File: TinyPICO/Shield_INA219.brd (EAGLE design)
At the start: 31.9 x 17.8 mm, 13 parts, among them J1 3.5mm, U1 INA219BIDCNT

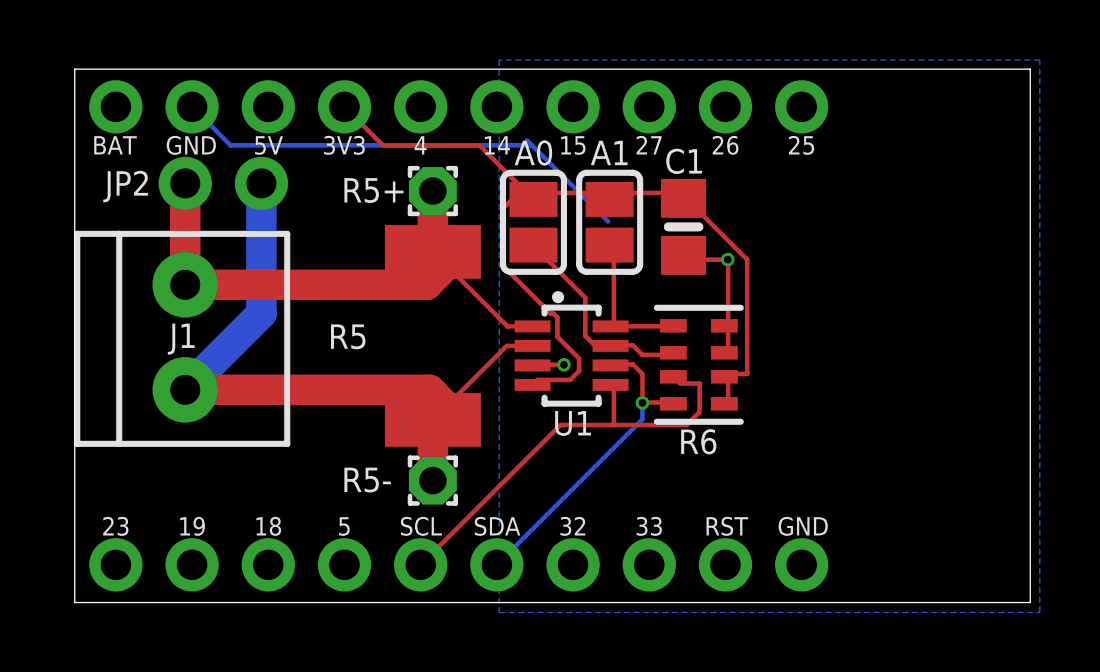
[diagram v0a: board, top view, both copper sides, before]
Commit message: TinyPICO Shield Ammeter INA219 v2.1
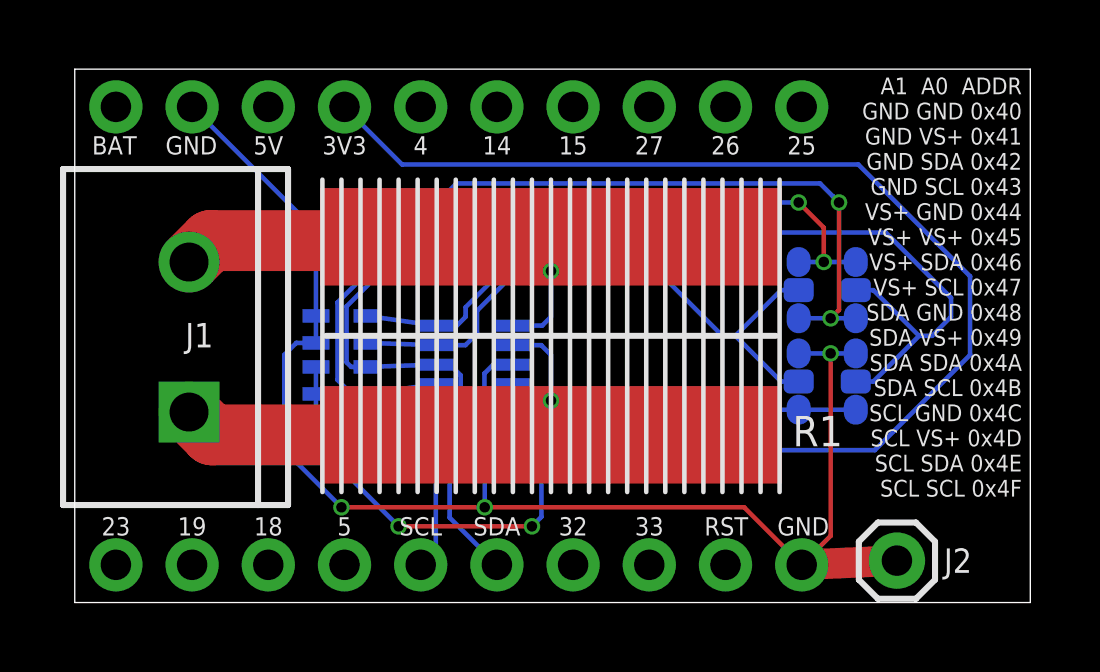
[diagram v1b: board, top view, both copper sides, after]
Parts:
- removed A0, A1: (no value), microbuilder:SOLDERJUMPER_REFLOW_NOPASTE
- removed JP2: (no value), microbuilder:1X02_ROUND
- removed R5: 0.1/1% (PT2512FK-070R1L), microbuilder:2512
- removed R5+, R5-: (no value), wirepad:1,6/0,9
- removed R6: 10K, microbuilder:RESPACK_4X0603
- added J2: (no value), SparkFun-Connectors:1X01
- added JMPA0.0, JMPA0.1, JMPA1.0, JMPA1.1: 0R-JUMPD, pv_jump-0r-smd:C0R-JMP_NONE
- added R1: FCSL150R025FER, pv:RESC90152X87N
- added R2: 10K, microbuilder:RESPACK_4X0603
- J1: value 3.5mm -> 5mm; device microbuilder:TERMBLOCK_1X2-3.5MM -> SparkFun-Connectors:SCREWTERMINAL-5MM-2
- moved C1 9.37 mm to (14.6, 5.08), flipped to the bottom, turned to 0 degrees
- moved U1 3.23 mm to (13.3, 8.26), flipped to the bottom
- moved J1 2.54 mm to (3.81, 6.35), turned to 90 degrees
- moved LOGO1 0.82 mm to (28.3, 15.9)
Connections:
- removed net N$1: A1.2, R6.1, U1.8
- removed net N$2: A0.2, R6.2, U1.7
- removed net VIN1+: J1.2, JP2.2, R5+.1, R5.2, U1.1
- removed net VIN1-: J1.1, JP2.1, R5-.1, R5.1, U1.2
- new net A0: JMPA0.0.2, JMPA0.1.2, R2.2, U1.7
- new net A1: JMPA1.0.2, JMPA1.1.2, R2.1, U1.8
- new net VIN+: J1.2, R1.2, U1.1
- new net VIN-: J1.1, R1.1, U1.2
- net 3.3V: now also JMPA0.0.1, JMPA1.0.1, R2.5, R2.6; no longer A0.1, A1.1, R6.5, R6.6
- net GND: now also J2.1, JMPA0.0.3, JMPA1.0.3, R2.7, R2.8; no longer R6.7, R6.8
- net SCL: now also JMPA0.1.1, JMPA1.1.1, R2.4; no longer R6.3
- net SDA: now also JMPA0.1.3, JMPA1.1.3, R2.3; no longer R6.4
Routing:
- net 3.3V: track 31.6 -> 68.6 mm, vias 0 -> 2
- net GND: track 21.7 -> 51.1 mm, vias 2 -> 3
- net A1: track 0.00 -> 29.3 mm
- net VIN1-: track 25.9 -> 0.00 mm
- net SDA: track 10.6 -> 33.7 mm, vias 1 -> 2
- net SCL: track 14.8 -> 36.8 mm, vias 0 -> 2
- net VIN1+: track 21.8 -> 0.00 mm
- net A0: track 0.00 -> 20.9 mm
- net VIN+: track 0.00 -> 15.6 mm, vias 0 -> 1
- net VIN-: track 0.00 -> 15.3 mm, vias 0 -> 1
- net N$2: track 6.96 -> 0.00 mm
- net N$1: track 4.85 -> 0.00 mm
- removed copper zone on layer 16, net GND
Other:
- board text added: "+ve"
- board text added: "-ve"
- board text added: "A0"
- board text added: "A1"
- board text added: "A1 A0 ADDR GND GND 0x40 GND VS+ 0x41 GND SDA 0x42 GND SCL 0x43 VS+ GND 0x44 VS+ VS+ 0x45 VS+ SDA 0x46 VS+ SCL 0x47 SDA GND 0x48 SDA VS+ 0x49 SDA SDA 0x4A SDA SCL 0x4B SCL GND 0x4C SCL VS+ 0x4D SCL SDA 0x4E SCL SCL 0x4F"
- board text added: "AMMETER SHIELD v2.1"
- board text added: "VS+"
- board text added: "load"
- board text removed: "INA219 SHIELD v1"
